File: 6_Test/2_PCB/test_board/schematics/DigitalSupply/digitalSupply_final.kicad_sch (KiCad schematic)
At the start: 10 parts, among them U4 LDO_Digital_Supply

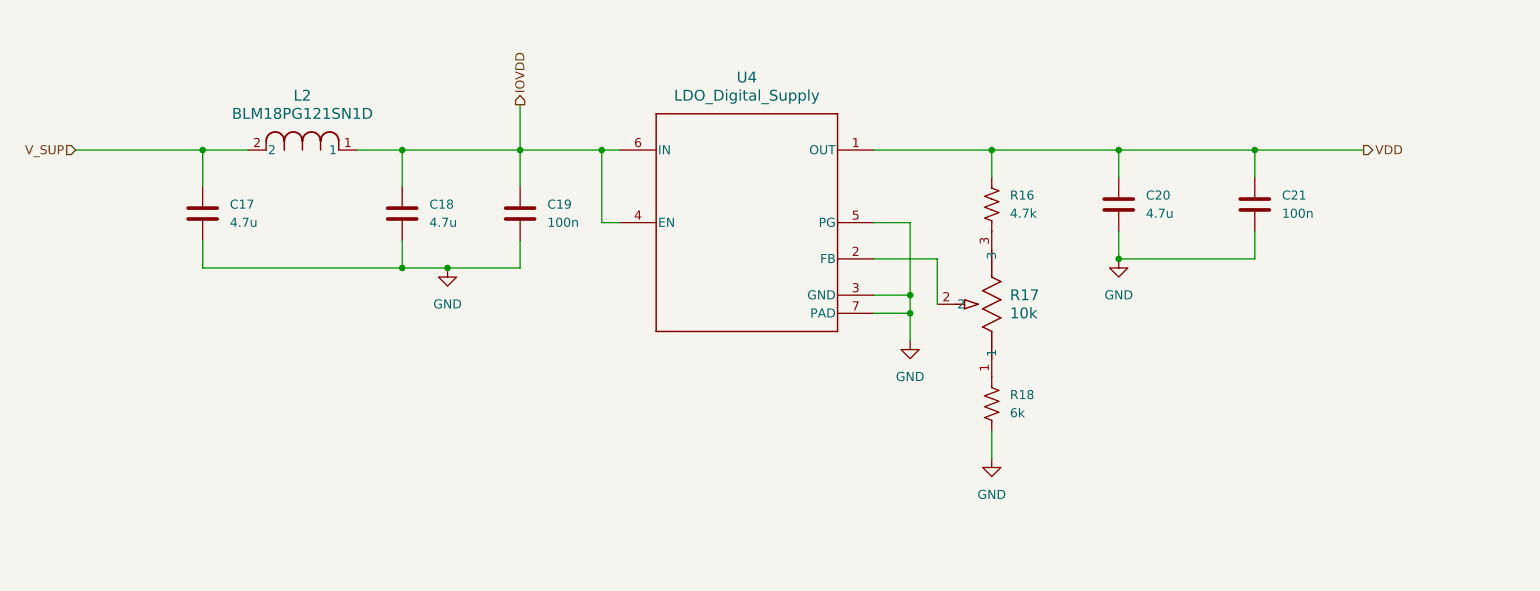
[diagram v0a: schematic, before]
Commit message: Revert "Corrections to schematic 11_20_24"
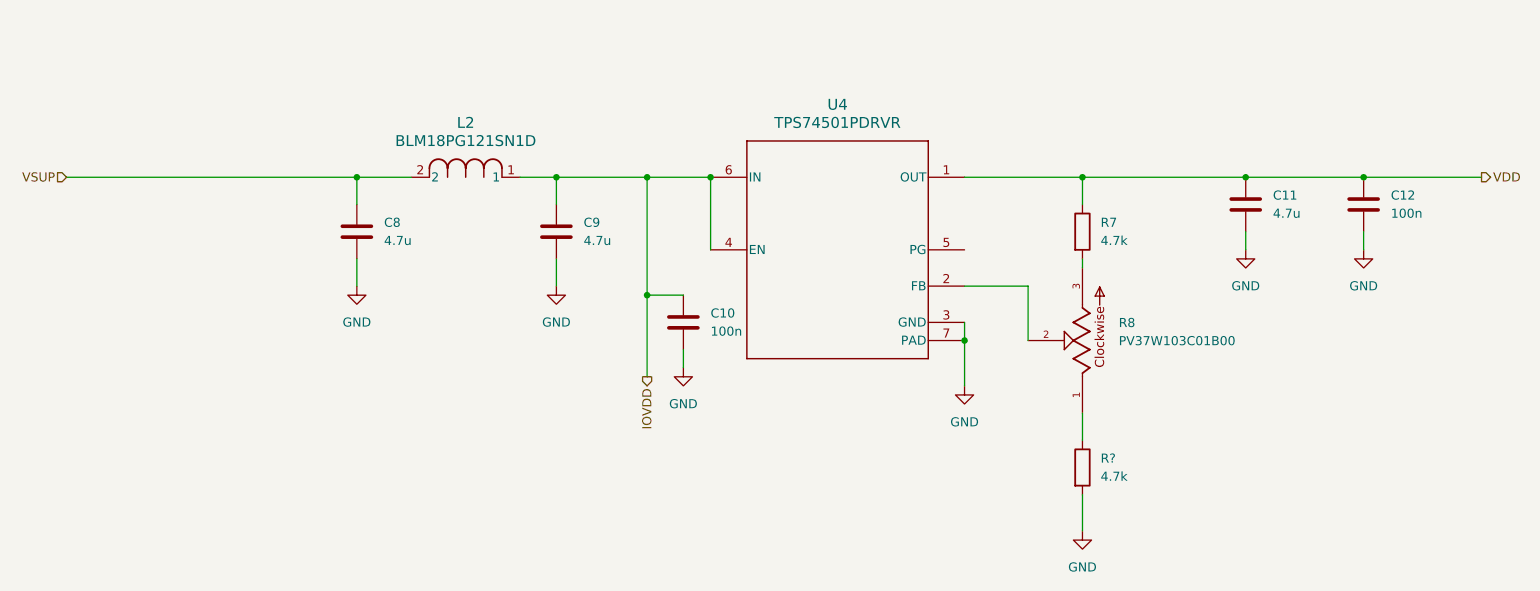
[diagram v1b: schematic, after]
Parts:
- removed C17, C18, C20: 4.7u, Capacitor_SMD:C_0201_0603Metric, symbol Device:C
- removed C19, C21: 100n, Capacitor_SMD:C_0201_0603Metric, symbol Device:C
- removed L2: BLM18PG121SN1D, ferriteBead120OhmFootprints:IND_BLM18_0603_MUR, symbol ferritebead:BLM18PG121SN1D
- removed R16: 4.7k, Resistor_SMD:R_0201_0603Metric, symbol Device:R_US
- removed R17: 10k, potentiometer_10turn:potentiometer_10turn, symbol pot10turn:PV37W103C01B00
- removed R18: 6k, Resistor_SMD:R_0201_0603Metric, symbol Device:R_US
- removed U4: LDO_Digital_Supply, tps745Footprints:DRV0006A_NV, symbol tps745:TPS74501PDRVR
- added C10, C12: 100n, Capacitor_SMD:C_0402_1005Metric, symbol Device:C
- added C11, C8, C9: 4.7u, Capacitor_SMD:C_0603_1608Metric, symbol Device:C
- added L2: BLM18PG121SN1D, IND_BLM18_0603_MUR, symbol 2024-09-16_06-39-17:BLM18PG121SN1D
- added R7, R?: 4.7k, symbol Device:R
- added R8: PV37W103C01B00, PV37W103C01B00:TRIM_PV37W103C01B00, symbol pot_10turn:PV37W103C01B00
- added U4: TPS74501PDRVR, DRV0006A, symbol TPS745_LDO:TPS74501PDRVR
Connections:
- net GND: now also C10.2, C11.2, C12.2, C8.2, C9.2, R?.2, U4.3 (GND), U4.7 (PAD)
- net IOVDD: now also C10.1, C9.1, L2.1, U4.4 (EN), U4.6 (IN)
- net VDD: now also C11.1, C12.1, R7.1, U4.1 (OUT)
- new net: R8.1, R?.1
- new net: R8.2, U4.2 (FB)
- new net: R7.2, R8.3
- new net VSUP: C8.1, L2.2

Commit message: Edits 112524
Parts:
- removed C11: 4.7u, Capacitor_SMD:C_0603_1608Metric, symbol Device:C
- removed C12: 100n, Capacitor_SMD:C_0402_1005Metric, symbol Device:C
- removed R7, R?: 4.7k, symbol Device:R
- added R7: 1k, ECE628_lib:resistor4.7k, symbol Device:R_US
- added R9: 4.7k, ECE628_lib:resistor4.7k, symbol Device:R_US
- C10: footprint Capacitor_SMD:C_0402_1005Metric -> cap100nFFootprints:CAP_CL05_SAM
- L2: footprint IND_BLM18_0603_MUR -> ferriteBead120OhmFootprints:IND_BLM18_0603_MUR
- R8: value PV37W103C01B00 -> 10k; footprint PV37W103C01B00:TRIM_PV37W103C01B00 -> ECE628_lib:potentiometer_10turn
- U4: footprint DRV0006A -> tps745Footprints:DRV0006A
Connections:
- net GND: now also R9.2
- net VDD: now also R7.1
- net at R8.2, U4.2 (FB): now also R9.1
- net at R8.3: now also R7.2
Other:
- moved on the sheet: C10, C8, C9, L2, R8, U4
